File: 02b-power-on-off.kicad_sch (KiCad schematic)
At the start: 13 parts, among them Q1 DMG2305UX-7, Q2 DMG2305UX-7, Q3 BSS138, SW0 SW_Push

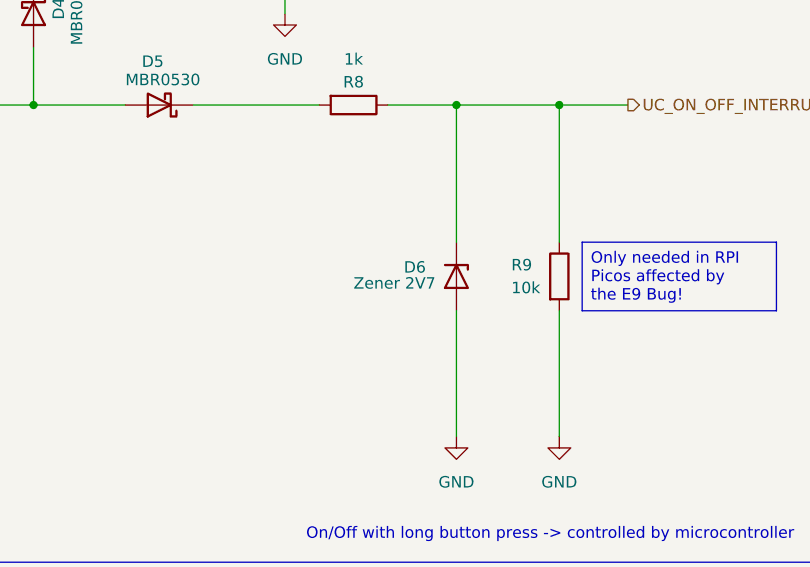
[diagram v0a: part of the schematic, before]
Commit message: Updated zener diode footprint
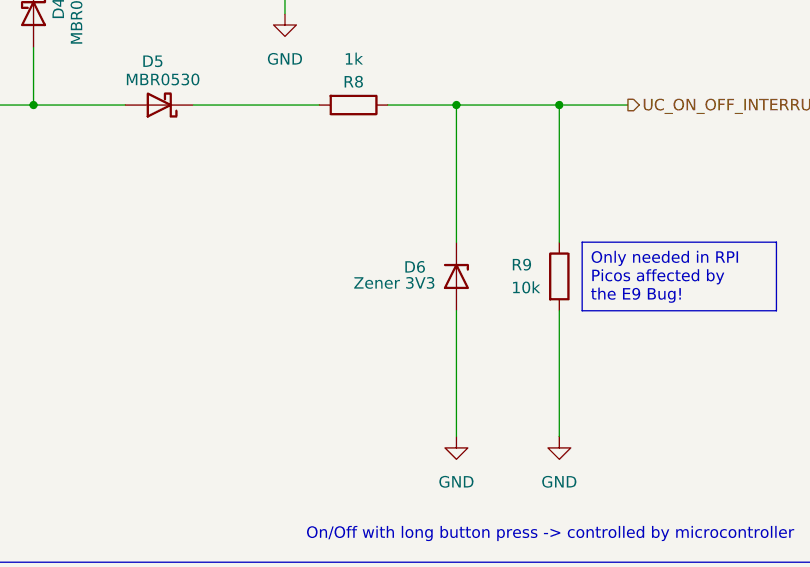
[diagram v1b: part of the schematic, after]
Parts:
- D6: value Zener 2V7 -> Zener 3V3; footprint Diode_SMD:D_1206_3216Metric_Pad1.42x1.75mm_HandSolder -> Diode_SMD:D_SOD-923
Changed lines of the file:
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@@
 			)
 		)
-		(property "Value" "Zener 2V7"
+		(property "Value" "Zener 3V3"
 			(at 198.12 121.412 90)
 			(effects
@@
 			)
 		)
-		(property "Footprint" "Diode_SMD:D_1206_3216Metric_Pad1.42x1.75mm_HandSolder"
+		(property "Footprint" "Diode_SMD:D_SOD-923"
 			(at 209.55 120.65 0)
 			(effects
@@
 			)
 		)
-		(property "Datasheet" "~"
+		(property "Datasheet" "https://fscdn.rohm.com/en/products/databook/datasheet/discrete/diode/zener/cdzvt2r3.0b-e.pdf"
 			(at 209.55 120.65 0)
 			(effects

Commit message: Reworked the PCB after review
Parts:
- SW5: renamed from SW0; footprint Button_Switch_THT:SW_PUSH_6mm -> Button_Switch_SMD:SW_Push_1P1T_NO_E-Switch_TL3301NxxxxxG
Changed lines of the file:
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@@
 		(stroke
 			(width 0)
-			(type default)
+			(type solid)
 		)
 		(fill
@@
 			)
 			(justify left top)
+			(href "https://datasheets.raspberrypi.com/pico/pico-2-datasheet.pdf")
 		)
 	)
@@
 		(dnp no)
 		(fields_autoplaced yes)
-		(property "Reference" "SW0"
+		(property "Reference" "SW5"
 			(at 152.4 93.98 0)
 			(effects
@@
 			)
 		)
-		(property "Footprint" "Button_Switch_THT:SW_PUSH_6mm"
+		(property "Footprint" "Button_Switch_SMD:SW_Push_1P1T_NO_E-Switch_TL3301NxxxxxG"
 			(at 152.4 96.52 0)
 			(effects
@@
 			)
 		)
-		(property "Datasheet" "~"
+		(property "Datasheet" "https://www.digikey.de/de/products/detail/e-switch/TL3301NF100QG/1805569"
 			(at 152.4 96.52 0)
 			(effects
@@
 			(project "ZEReader-Pico"
 				(path "/ec954637-2a8b-4662-b4a1-f88107f11cb0/a3bedda0-cdd4-4cf1-8725-53db0608a498"
-					(reference "SW0")
+					(reference "SW5")
 					(unit 1)
 				)

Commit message: Bigger Zener, improved BoM, general improvements
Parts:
- C3: DigiKey (none) -> 1276-1804-1-ND; Manufacturer PartNo (none) -> CL31B106KAHNNNE
- D3, D4, D5: DigiKey (none) -> MBR0530T1GOSCT-ND; Manufacturer PartNo (none) -> MBR0530T1G
- D6: footprint Diode_SMD:D_SOD-923 -> Diode_SMD:Nexperia_CFP3_SOD-123W; DigiKey (none) -> TFZVTR3.3BCT-ND; Manufacturer PartNo (none) -> TFZVTR3.3B
- Q1, Q2: DigiKey (none) -> DMG2305UX-7DICT-ND; Manufacturer PartNo (none) -> DMG2305UX-7
- Q3: DigiKey (none) -> BSS138LT3GOSCT-ND; Manufacturer PartNo (none) -> BSS138LT3G
- R7, R9: DigiKey (none) -> 311-10.0KFRCT-ND; Manufacturer PartNo (none) -> RC1206FR-0710KL
- R8: DigiKey (none) -> RNCP1206FTD1K00CT-ND; Manufacturer PartNo (none) -> RNCP1206FTD1K00
- SW5: DigiKey (none) -> EG6054CT-ND; Manufacturer PartNo (none) -> TL3301NF100QG
